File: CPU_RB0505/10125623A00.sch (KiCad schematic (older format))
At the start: 0 parts

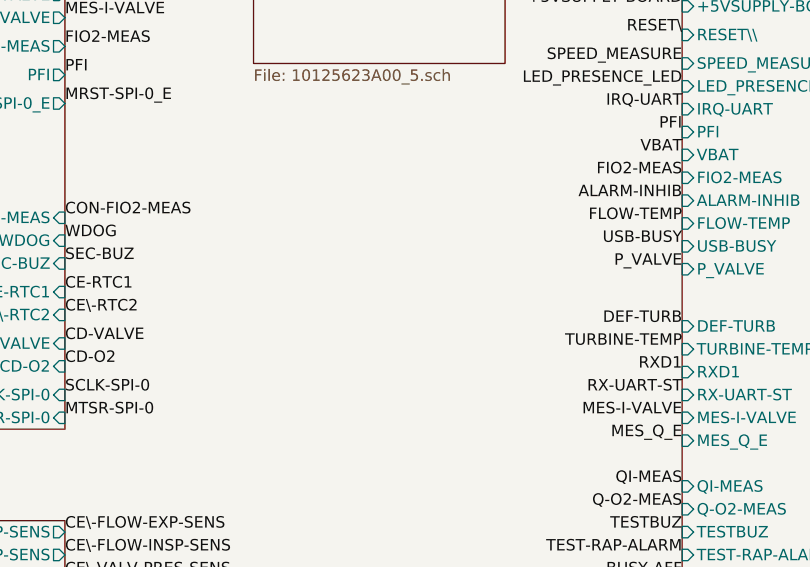
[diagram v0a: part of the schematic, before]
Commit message: add through holes as symbols
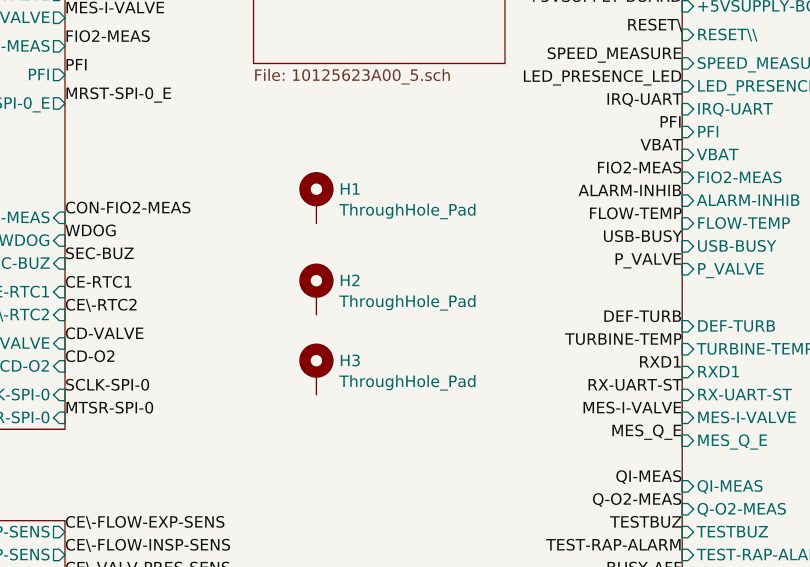
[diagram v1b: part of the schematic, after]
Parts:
- added H1, H2, H3: ThroughHole_Pad, symbol Mechanical:MountingHole_Pad
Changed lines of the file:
@@
 Wire Bus Line
 	7150 5000 6950 5000
+$Comp
+L Mechanical:MountingHole_Pad H1
+U 1 1 5E9B6535
+P 3050 2100
+F 0 "H1" H 3150 2149 50  0000 L CNN
+F 1 "ThroughHole_Pad" H 3150 2058 50  0000 L CNN
+F 2 "" H 3050 2100 50  0001 C CNN
+F 3 "~" H 3050 2100 50  0001 C CNN
+	1    3050 2100
+	1    0    0    -1
+$EndComp
+$Comp
+L Mechanical:MountingHole_Pad H2
+U 1 1 5E9B69D4
+P 3050 2500
+F 0 "H2" H 3150 2549 50  0000 L CNN
+F 1 "ThroughHole_Pad" H 3150 2458 50  0000 L CNN
+F 2 "" H 3050 2500 50  0001 C CNN
+F 3 "~" H 3050 2500 50  0001 C CNN
+	1    3050 2500
+	1    0    0    -1
+$EndComp
+$Comp
+L Mechanical:MountingHole_Pad H3
+U 1 1 5E9B6C7F
+P 3050 2850
+F 0 "H3" H 3150 2899 50  0000 L CNN
+F 1 "ThroughHole_Pad" H 3150 2808 50  0000 L CNN
+F 2 "" H 3050 2850 50  0001 C CNN
+F 3 "~" H 3050 2850 50  0001 C CNN
+	1    3050 2850
+	1    0    0    -1
+$EndComp
 $EndSCHEMATC

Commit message: back anotate from cmp file
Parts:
- H1, H3: footprint (none) -> AllModules:ThroughHole_60milx12mil_Pad_Cu_Mask
- H2: footprint (none) -> AllModules:ThroughHole_60milx6mm_Pad_Cu_Mask
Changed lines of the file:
@@
 F 0 "H1" H 3150 2149 50  0000 L CNN
 F 1 "ThroughHole_Pad" H 3150 2058 50  0000 L CNN
-F 2 "" H 3050 2100 50  0001 C CNN
+F 2 "AllModules:ThroughHole_60milx12mil_Pad_Cu_Mask" H 3050 2100 50  0001 C CNN
 F 3 "~" H 3050 2100 50  0001 C CNN
 	1    3050 2100
@@
 F 0 "H2" H 3150 2549 50  0000 L CNN
 F 1 "ThroughHole_Pad" H 3150 2458 50  0000 L CNN
-F 2 "" H 3050 2500 50  0001 C CNN
+F 2 "AllModules:ThroughHole_60milx6mm_Pad_Cu_Mask" H 3050 2500 50  0001 C CNN
 F 3 "~" H 3050 2500 50  0001 C CNN
 	1    3050 2500
@@
 F 0 "H3" H 3150 2899 50  0000 L CNN
 F 1 "ThroughHole_Pad" H 3150 2808 50  0000 L CNN
-F 2 "" H 3050 2850 50  0001 C CNN
+F 2 "AllModules:ThroughHole_60milx12mil_Pad_Cu_Mask" H 3050 2850 50  0001 C CNN
 F 3 "~" H 3050 2850 50  0001 C CNN
 	1    3050 2850

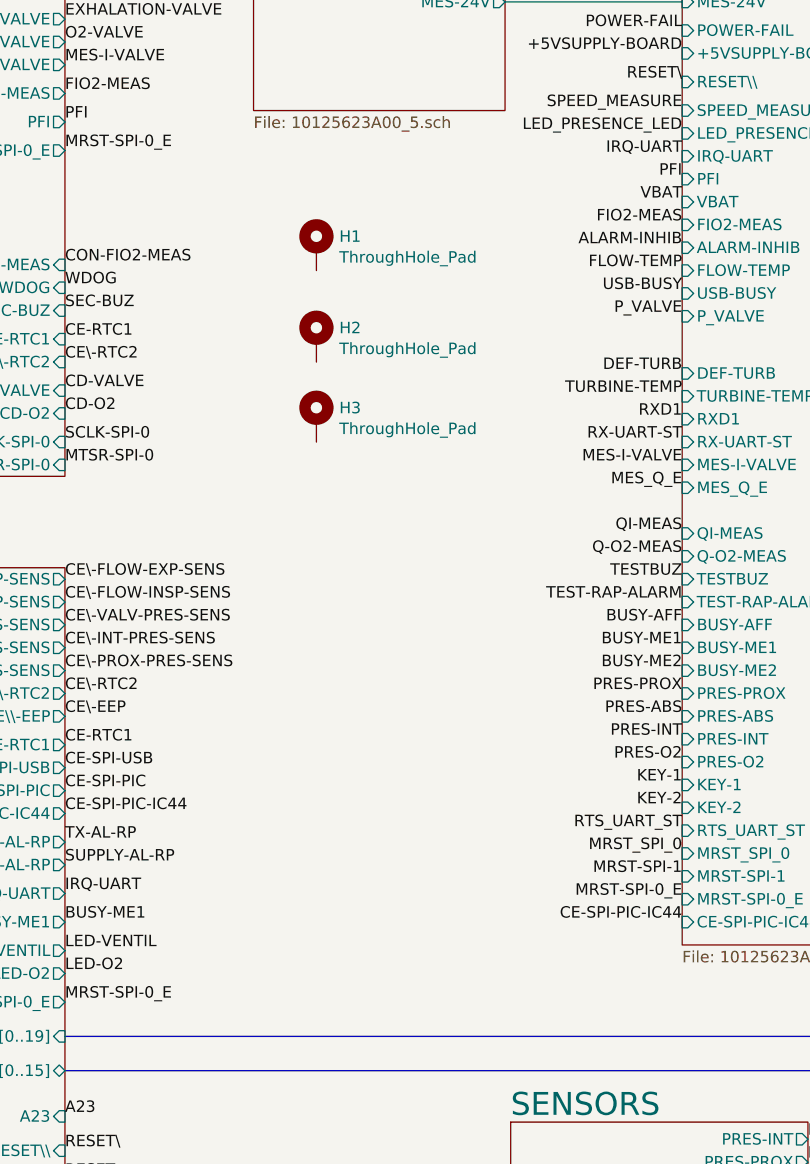
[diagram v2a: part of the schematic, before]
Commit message: add mounting holes to schematic
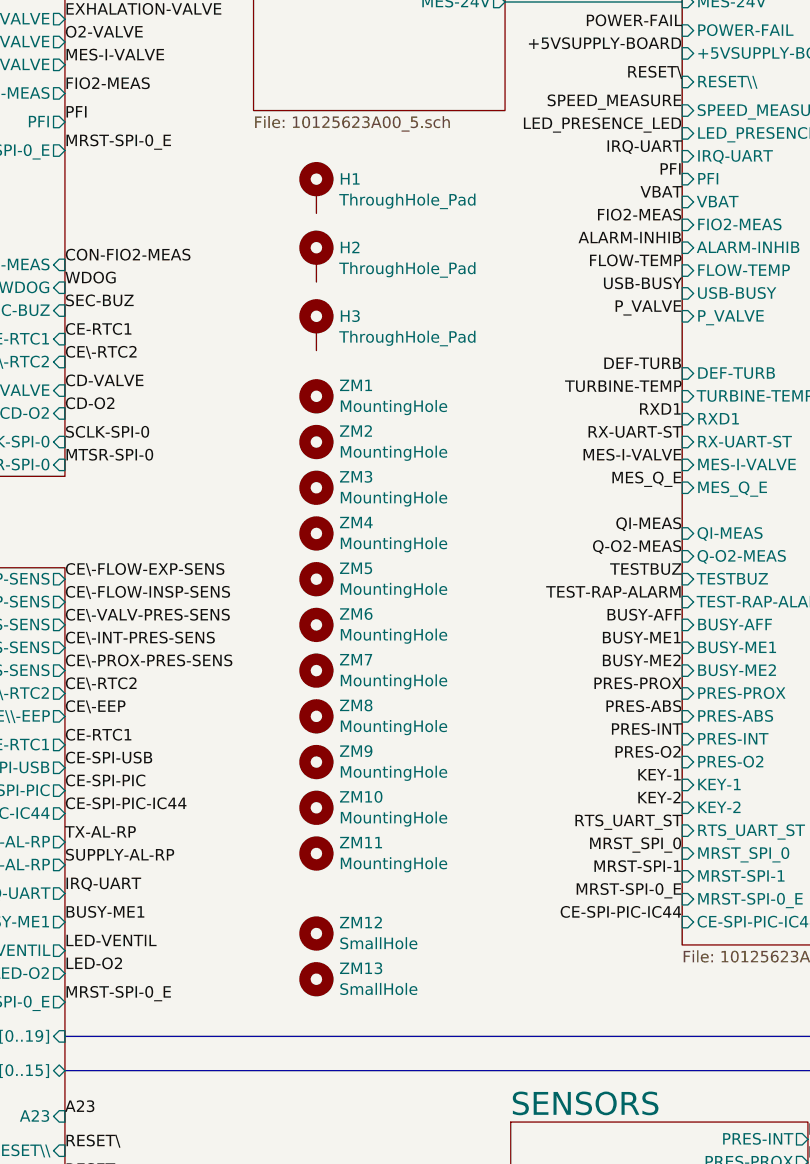
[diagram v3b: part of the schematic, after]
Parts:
- added ZM1, ZM10, ZM11, ZM2, ZM3, ZM4, ZM5, ZM6, ZM7, ZM8, ZM9: MountingHole, AllModules:FIX35_1, symbol Mechanical:MountingHole
- added ZM12, ZM13: SmallHole, AllModules:FIX30_1, symbol Mechanical:MountingHole
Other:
- moved on the sheet: H1, H2, H3
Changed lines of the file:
@@
 L Mechanical:MountingHole_Pad H1
 U 1 1 5E9B6535
-P 3050 2100
-F 0 "H1" H 3150 2149 50  0000 L CNN
-F 1 "ThroughHole_Pad" H 3150 2058 50  0000 L CNN
-F 2 "AllModules:ThroughHole_60milx12mil_Pad_Cu_Mask" H 3050 2100 50  0001 C CNN
-F 3 "~" H 3050 2100 50  0001 C CNN
-	1    3050 2100
+P 3050 1850
+F 0 "H1" H 3150 1899 50  0000 L CNN
+F 1 "ThroughHole_Pad" H 3150 1808 50  0000 L CNN
+F 2 "AllModules:ThroughHole_60milx12mil_Pad_Cu_Mask" H 3050 1850 50  0001 C CNN
+F 3 "~" H 3050 1850 50  0001 C CNN
+	1    3050 1850
 	1    0    0    -1
 $EndComp
@@
 L Mechanical:MountingHole_Pad H2
 U 1 1 5E9B69D4
-P 3050 2500
-F 0 "H2" H 3150 2549 50  0000 L CNN
-F 1 "ThroughHole_Pad" H 3150 2458 50  0000 L CNN
-F 2 "AllModules:ThroughHole_60milx6mm_Pad_Cu_Mask" H 3050 2500 50  0001 C CNN
-F 3 "~" H 3050 2500 50  0001 C CNN
-	1    3050 2500
+P 3050 2150
+F 0 "H2" H 3150 2199 50  0000 L CNN
+F 1 "ThroughHole_Pad" H 3150 2108 50  0000 L CNN
+F 2 "AllModules:ThroughHole_60milx6mm_Pad_Cu_Mask" H 3050 2150 50  0001 C CNN
+F 3 "~" H 3050 2150 50  0001 C CNN
+	1    3050 2150
 	1    0    0    -1
 $EndComp
@@
 L Mechanical:MountingHole_Pad H3
 U 1 1 5E9B6C7F
-P 3050 2850
-F 0 "H3" H 3150 2899 50  0000 L CNN
-F 1 "ThroughHole_Pad" H 3150 2808 50  0000 L CNN
-F 2 "AllModules:ThroughHole_60milx12mil_Pad_Cu_Mask" H 3050 2850 50  0001 C CNN
-F 3 "~" H 3050 2850 50  0001 C CNN
-	1    3050 2850
+P 3050 2450
+F 0 "H3" H 3150 2499 50  0000 L CNN
+F 1 "ThroughHole_Pad" H 3150 2408 50  0000 L CNN
+F 2 "AllModules:ThroughHole_60milx12mil_Pad_Cu_Mask" H 3050 2450 50  0001 C CNN
+F 3 "~" H 3050 2450 50  0001 C CNN
+	1    3050 2450
 	1    0    0    -1
 $EndComp
+$Comp
+L Mechanical:MountingHole ZM1
+U 1 1 5EA72855
+P 3050 2750
+F 0 "ZM1" H 3150 2796 50  0000 L CNN
+F 1 "MountingHole" H 3150 2705 50  0000 L CNN
+F 2 "AllModules:FIX35_1" H 3050 2750 50  0001 C CNN
+F 3 "~" H 3050 2750 50  0001 C CNN
+	1    3050 2750
+	1    0    0    -1
+$EndComp
+$Comp
+L Mechanical:MountingHole ZM2
+U 1 1 5EA7D06E
+P 3050 2950
+F 0 "ZM2" H 3150 2996 50  0000 L CNN
+F 1 "MountingHole" H 3150 2905 50  0000 L CNN
+F 2 "AllModules:FIX35_1" H 3050 2950 50  0001 C CNN
+F 3 "~" H 3050 2950 50  0001 C CNN
+	1    3050 2950
+	1    0    0    -1
+$EndComp
+$Comp
+L Mechanical:MountingHole ZM3
+U 1 1 5EA7DBDF
+P 3050 3150
+F 0 "ZM3" H 3150 3196 50  0000 L CNN
+F 1 "MountingHole" H 3150 3105 50  0000 L CNN
+F 2 "AllModules:FIX35_1" H 3050 3150 50  0001 C CNN
+F 3 "~" H 3050 3150 50  0001 C CNN
+	1    3050 3150
+	1    0    0    -1
+$EndComp
+$Comp
+L Mechanical:MountingHole ZM4
+U 1 1 5EA7DBE9
+P 3050 3350
+F 0 "ZM4" H 3150 3396 50  0000 L CNN
+F 1 "MountingHole" H 3150 3305 50  0000 L CNN
+F 2 "AllModules:FIX35_1" H 3050 3350 50  0001 C CNN
+F 3 "~" H 3050 3350 50  0001 C CNN
+	1    3050 3350
+	1    0    0    -1
+$EndComp
+$Comp
+L Mechanical:MountingHole ZM5
+U 1 1 5EA7E64F
+P 3050 3550
+F 0 "ZM5" H 3150 3596 50  0000 L CNN
+F 1 "MountingHole" H 3150 3505 50  0000 L CNN
+F 2 "AllModules:FIX35_1" H 3050 3550 50  0001 C CNN
+F 3 "~" H 3050 3550 50  0001 C CNN
+	1    3050 3550
+	1    0    0    -1
+$EndComp
+$Comp
+L Mechanical:MountingHole ZM6
+U 1 1 5EA7E659
+P 3050 3750
+F 0 "ZM6" H 3150 3796 50  0000 L CNN
+F 1 "MountingHole" H 3150 3705 50  0000 L CNN
+F 2 "AllModules:FIX35_1" H 3050 3750 50  0001 C CNN
+F 3 "~" H 3050 3750 50  0001 C CNN
+	1    3050 3750
+	1    0    0    -1
+$EndComp
+$Comp
+L Mechanical:MountingHole ZM7
+U 1 1 5EA7E663
+P 3050 3950
+F 0 "ZM7" H 3150 3996 50  0000 L CNN
+F 1 "MountingHole" H 3150 3905 50  0000 L CNN
+F 2 "AllModules:FIX35_1" H 3050 3950 50  0001 C CNN
+F 3 "~" H 3050 3950 50  0001 C CNN
+	1    3050 3950
+	1    0    0    -1
+$EndComp
+$Comp
+L Mechanical:MountingHole ZM8
+U 1 1 5EA7E66D
+P 3050 4150
+F 0 "ZM8" H 3150 4196 50  0000 L CNN
+F 1 "MountingHole" H 3150 4105 50  0000 L CNN
+F 2 "AllModules:FIX35_1" H 3050 4150 50  0001 C CNN
+F 3 "~" H 3050 4150 50  0001 C CNN
+	1    3050 4150
+	1    0    0    -1
+$EndComp
+$Comp
+L Mechanical:MountingHole ZM9
+U 1 1 5EA85DD7
+P 3050 4350
+F 0 "ZM9" H 3150 4396 50  0000 L CNN
+F 1 "MountingHole" H 3150 4305 50  0000 L CNN
+F 2 "AllModules:FIX35_1" H 3050 4350 50  0001 C CNN
+F 3 "~" H 3050 4350 50  0001 C CNN
+	1    3050 4350
+	1    0    0    -1
+$EndComp
+$Comp
+L Mechanical:MountingHole ZM10
+U 1 1 5EA85DE1
+P 3050 4550
+F 0 "ZM10" H 3150 4596 50  0000 L CNN
+F 1 "MountingHole" H 3150 4505 50  0000 L CNN
+F 2 "AllModules:FIX35_1" H 3050 4550 50  0001 C CNN
+F 3 "~" H 3050 4550 50  0001 C CNN
+	1    3050 4550
+	1    0    0    -1
+$EndComp
+$Comp
+L Mechanical:MountingHole ZM11
+U 1 1 5EA85DEB
+P 3050 4750
+F 0 "ZM11" H 3150 4796 50  0000 L CNN
+F 1 "MountingHole" H 3150 4705 50  0000 L CNN
+F 2 "AllModules:FIX35_1" H 3050 4750 50  0001 C CNN
+F 3 "~" H 3050 4750 50  0001 C CNN
+	1    3050 4750
+	1    0    0    -1
+$EndComp
+$Comp
+L Mechanical:MountingHole ZM12
+U 1 1 5EA85DF5
+P 3050 5100
+F 0 "ZM12" H 3150 5146 50  0000 L CNN
+F 1 "SmallHole" H 3150 5055 50  0000 L CNN
+F 2 "AllModules:FIX30_1" H 3050 5100 50  0001 C CNN
+F 3 "~" H 3050 5100 50  0001 C CNN
+	1    3050 5100
+	1    0    0    -1
+$EndComp
+$Comp
+L Mechanical:MountingHole ZM13
+U 1 1 5EA87776
+P 3050 5300
+F 0 "ZM13" H 3150 5346 50  0000 L CNN
+F 1 "SmallHole" H 3150 5255 50  0000 L CNN
+F 2 "AllModules:FIX30_1" H 3050 5300 50  0001 C CNN
+F 3 "~" H 3050 5300 50  0001 C CNN
+	1    3050 5300
+	1    0    0    -1
+$EndComp

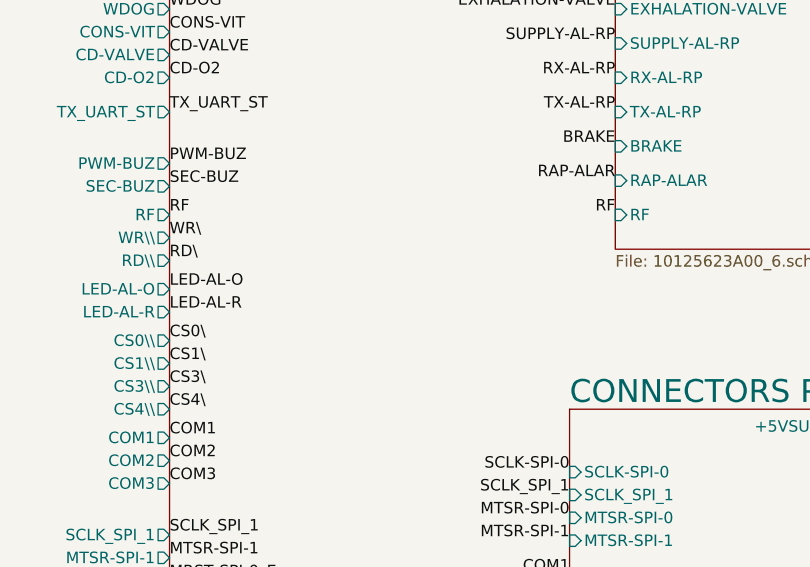
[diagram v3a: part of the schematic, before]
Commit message: add fiducials to schematic
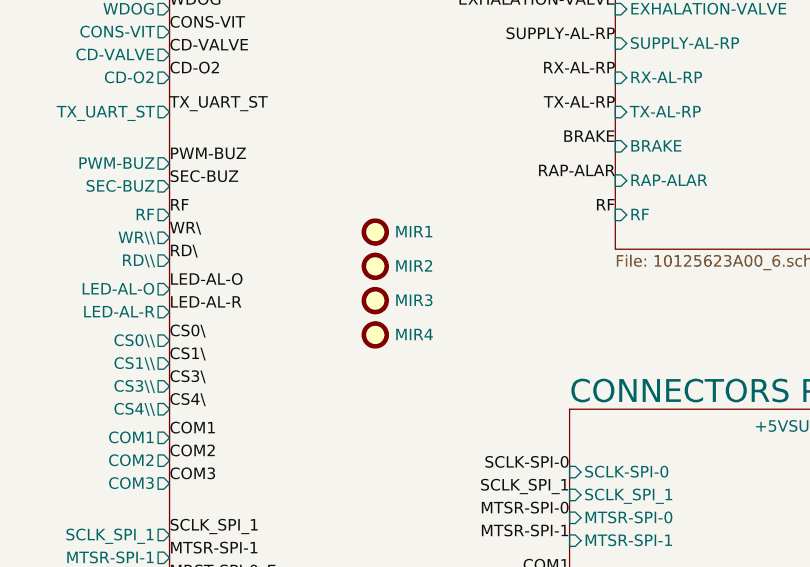
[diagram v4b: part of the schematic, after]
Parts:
- added MIR1, MIR2, MIR3, MIR4: Fiducial, AllModules:MIRECMS_D-1.5_1, symbol Mechanical:Fiducial
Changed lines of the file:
@@
+	1    0    0    -1
+$EndComp
+$Comp
+L Mechanical:Fiducial MIR1
+U 1 1 5E9BC652
+P 7850 2750
+F 0 "MIR1" H 7935 2750 50  0000 L CNN
+F 1 "Fiducial" H 7935 2705 50  0001 L CNN
+F 2 "AllModules:MIRECMS_D-1.5_1" H 7850 2750 50  0001 C CNN
+F 3 "~" H 7850 2750 50  0001 C CNN
+	1    7850 2750
+	1    0    0    -1
+$EndComp
+$Comp
+L Mechanical:Fiducial MIR2
+U 1 1 5E9BE4E3
+P 7850 2900
+F 0 "MIR2" H 7935 2900 50  0000 L CNN
+F 1 "Fiducial" H 7935 2855 50  0001 L CNN
+F 2 "AllModules:MIRECMS_D-1.5_1" H 7850 2900 50  0001 C CNN
+F 3 "~" H 7850 2900 50  0001 C CNN
+	1    7850 2900
+	1    0    0    -1
+$EndComp
+$Comp
+L Mechanical:Fiducial MIR3
+U 1 1 5E9BE6CC
+P 7850 3050
+F 0 "MIR3" H 7935 3050 50  0000 L CNN
+F 1 "Fiducial" H 7935 3005 50  0001 L CNN
+F 2 "AllModules:MIRECMS_D-1.5_1" H 7850 3050 50  0001 C CNN
+F 3 "~" H 7850 3050 50  0001 C CNN
+	1    7850 3050
+	1    0    0    -1
+$EndComp
+$Comp
+L Mechanical:Fiducial MIR4
+U 1 1 5E9BE945
+P 7850 3200
+F 0 "MIR4" H 7935 3200 50  0000 L CNN
+F 1 "Fiducial" H 7935 3155 50  0001 L CNN
+F 2 "AllModules:MIRECMS_D-1.5_1" H 7850 3200 50  0001 C CNN
+F 3 "~" H 7850 3200 50  0001 C CNN
+	1    7850 3200
 	1    0    0    -1
 $EndComp

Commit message: add marks to schematic
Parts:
- added CAM1, CAM2, CAM3: Fiducial, AllModules:PER-COVIDIEN_TEXTE_1, symbol Mechanical:Fiducial
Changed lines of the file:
@@
+	1    0    0    -1
+$EndComp
+$Comp
+L Mechanical:Fiducial CAM1
+U 1 1 5E9C1ED0
+P 7850 3450
+F 0 "CAM1" H 7935 3450 50  0000 L CNN
+F 1 "Fiducial" H 7935 3405 50  0001 L CNN
+F 2 "AllModules:PER-COVIDIEN_TEXTE_1" H 7850 3450 50  0001 C CNN
+F 3 "~" H 7850 3450 50  0001 C CNN
+	1    7850 3450
+	1    0    0    -1
+$EndComp
+$Comp
+L Mechanical:Fiducial CAM2
+U 1 1 5E9C238F
+P 7850 3600
+F 0 "CAM2" H 7935 3600 50  0000 L CNN
+F 1 "Fiducial" H 7935 3555 50  0001 L CNN
+F 2 "AllModules:PER-COVIDIEN_TEXTE_1" H 7850 3600 50  0001 C CNN
+F 3 "~" H 7850 3600 50  0001 C CNN
+	1    7850 3600
+	1    0    0    -1
+$EndComp
+$Comp
+L Mechanical:Fiducial CAM3
+U 1 1 5E9C260F
+P 7850 3750
+F 0 "CAM3" H 7935 3750 50  0000 L CNN
+F 1 "Fiducial" H 7935 3705 50  0001 L CNN
+F 2 "AllModules:PER-COVIDIEN_TEXTE_1" H 7850 3750 50  0001 C CNN
+F 3 "~" H 7850 3750 50  0001 C CNN
+	1    7850 3750
 	1    0    0    -1
 $EndComp

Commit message: fix marks fp of schematic
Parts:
- CAM1: footprint AllModules:PER-COVIDIEN_TEXTE_1 -> AllModules:A3_EQFS_COVIDIEN_1
- CAM2: footprint AllModules:PER-COVIDIEN_TEXTE_1 -> AllModules:A3_EQFC_COVIDIEN_1
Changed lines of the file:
@@
 F 0 "CAM1" H 7935 3450 50  0000 L CNN
 F 1 "Fiducial" H 7935 3405 50  0001 L CNN
-F 2 "AllModules:PER-COVIDIEN_TEXTE_1" H 7850 3450 50  0001 C CNN
+F 2 "AllModules:A3_EQFS_COVIDIEN_1" H 7850 3450 50  0001 C CNN
 F 3 "~" H 7850 3450 50  0001 C CNN
 	1    7850 3450
@@
 F 0 "CAM2" H 7935 3600 50  0000 L CNN
 F 1 "Fiducial" H 7935 3555 50  0001 L CNN
-F 2 "AllModules:PER-COVIDIEN_TEXTE_1" H 7850 3600 50  0001 C CNN
+F 2 "AllModules:A3_EQFC_COVIDIEN_1" H 7850 3600 50  0001 C CNN
 F 3 "~" H 7850 3600 50  0001 C CNN
 	1    7850 3600

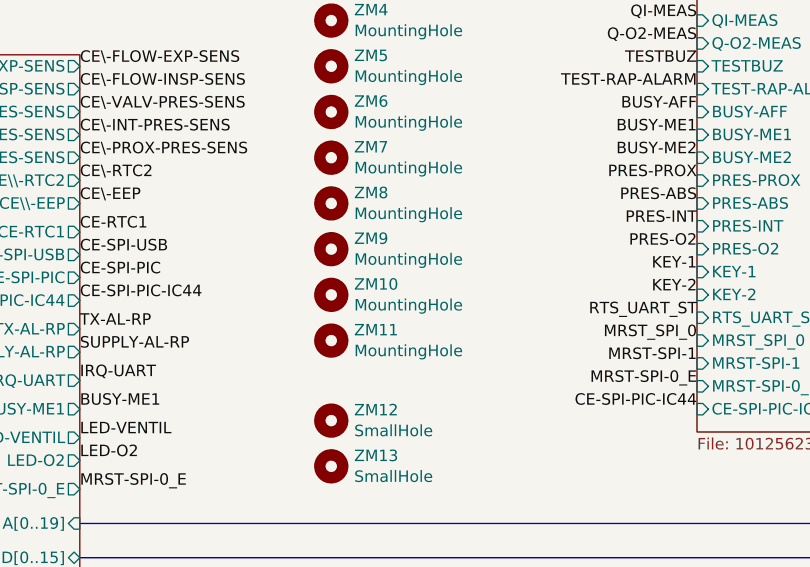
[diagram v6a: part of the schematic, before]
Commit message: add mounting holes, separate footprints from display
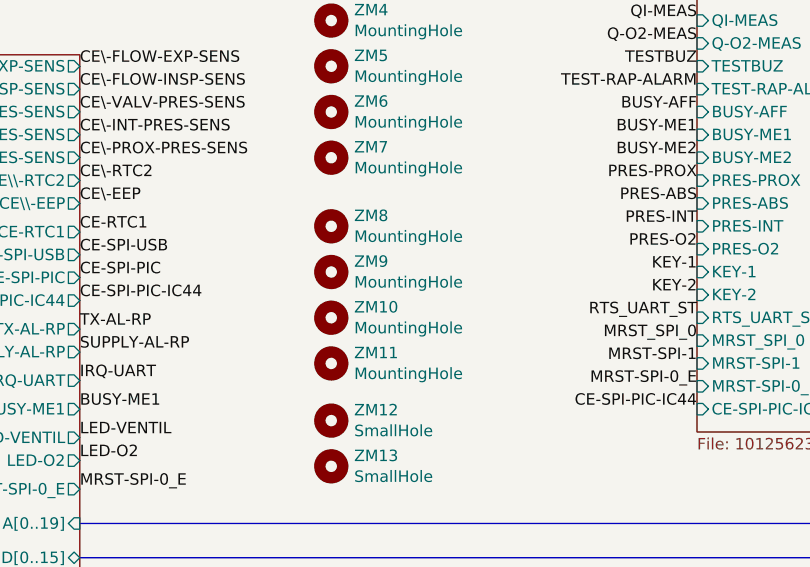
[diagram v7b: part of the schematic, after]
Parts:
- ZM10, ZM11, ZM8, ZM9: footprint AllModules:FIX35_1 -> AllModules:FIX35_1_display
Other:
- moved on the sheet: ZM10, ZM11, ZM8, ZM9
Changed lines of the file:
@@
 L Mechanical:MountingHole ZM8
 U 1 1 5EA7E66D
-P 3050 4150
-F 0 "ZM8" H 3150 4196 50  0000 L CNN
-F 1 "MountingHole" H 3150 4105 50  0000 L CNN
-F 2 "AllModules:FIX35_1" H 3050 4150 50  0001 C CNN
-F 3 "~" H 3050 4150 50  0001 C CNN
-	1    3050 4150
+P 3050 4250
+F 0 "ZM8" H 3150 4296 50  0000 L CNN
+F 1 "MountingHole" H 3150 4205 50  0000 L CNN
+F 2 "AllModules:FIX35_1_display" H 3050 4250 50  0001 C CNN
+F 3 "~" H 3050 4250 50  0001 C CNN
+	1    3050 4250
 	1    0    0    -1
 $EndComp
@@
 L Mechanical:MountingHole ZM9
 U 1 1 5EA85DD7
-P 3050 4350
-F 0 "ZM9" H 3150 4396 50  0000 L CNN
-F 1 "MountingHole" H 3150 4305 50  0000 L CNN
-F 2 "AllModules:FIX35_1" H 3050 4350 50  0001 C CNN
-F 3 "~" H 3050 4350 50  0001 C CNN
-	1    3050 4350
+P 3050 4450
+F 0 "ZM9" H 3150 4496 50  0000 L CNN
+F 1 "MountingHole" H 3150 4405 50  0000 L CNN
+F 2 "AllModules:FIX35_1_display" H 3050 4450 50  0001 C CNN
+F 3 "~" H 3050 4450 50  0001 C CNN
+	1    3050 4450
 	1    0    0    -1
 $EndComp
@@
 L Mechanical:MountingHole ZM10
 U 1 1 5EA85DE1
-P 3050 4550
-F 0 "ZM10" H 3150 4596 50  0000 L CNN
-F 1 "MountingHole" H 3150 4505 50  0000 L CNN
-F 2 "AllModules:FIX35_1" H 3050 4550 50  0001 C CNN
-F 3 "~" H 3050 4550 50  0001 C CNN
-	1    3050 4550
+P 3050 4650
+F 0 "ZM10" H 3150 4696 50  0000 L CNN
+F 1 "MountingHole" H 3150 4605 50  0000 L CNN
+F 2 "AllModules:FIX35_1_display" H 3050 4650 50  0001 C CNN
+F 3 "~" H 3050 4650 50  0001 C CNN
+	1    3050 4650
 	1    0    0    -1
 $EndComp
@@
 L Mechanical:MountingHole ZM11
 U 1 1 5EA85DEB
-P 3050 4750
-F 0 "ZM11" H 3150 4796 50  0000 L CNN
-F 1 "MountingHole" H 3150 4705 50  0000 L CNN
-F 2 "AllModules:FIX35_1" H 3050 4750 50  0001 C CNN
-F 3 "~" H 3050 4750 50  0001 C CNN
-	1    3050 4750
+P 3050 4850
+F 0 "ZM11" H 3150 4896 50  0000 L CNN
+F 1 "MountingHole" H 3150 4805 50  0000 L CNN
+F 2 "AllModules:FIX35_1_display" H 3050 4850 50  0001 C CNN
+F 3 "~" H 3050 4850 50  0001 C CNN
+	1    3050 4850
 	1    0    0    -1
 $EndComp
